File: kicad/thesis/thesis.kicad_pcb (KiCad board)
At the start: 2 copper layers, 50 x 49 mm, 13 parts, among them Q1 IRLZB8721, SW1 SW_DIP_x01, U1 INA219AxD

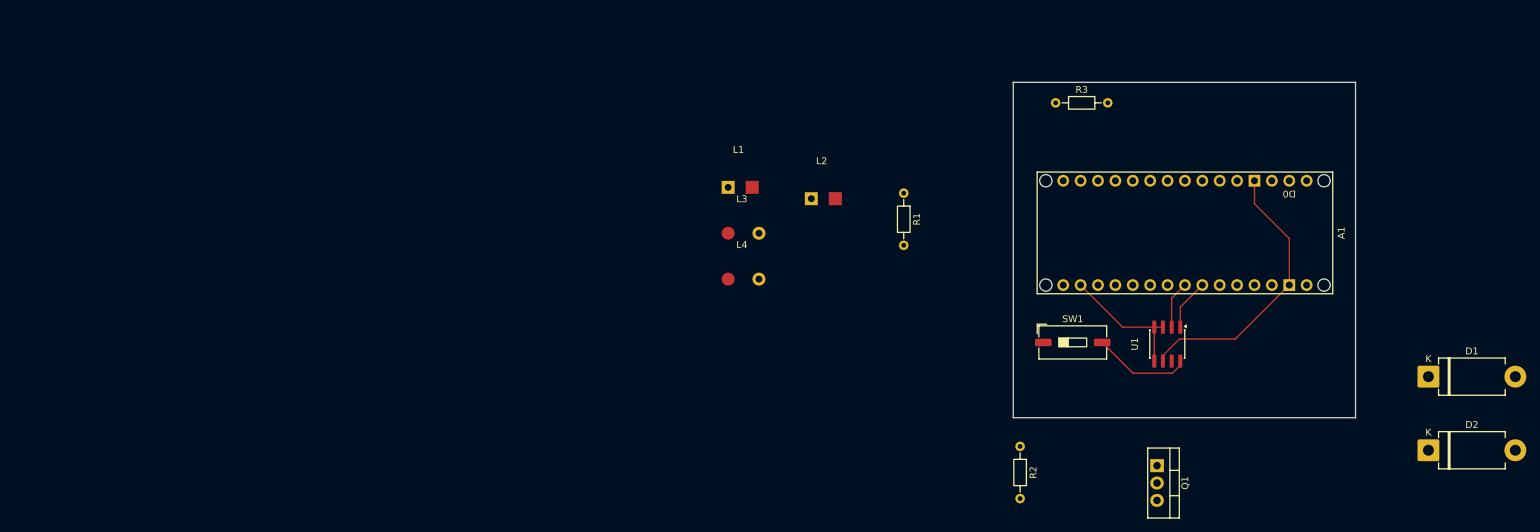
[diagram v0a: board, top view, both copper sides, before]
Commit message: Changed the PCB design
85mm x 60mm dimensions for the initial PCB layout
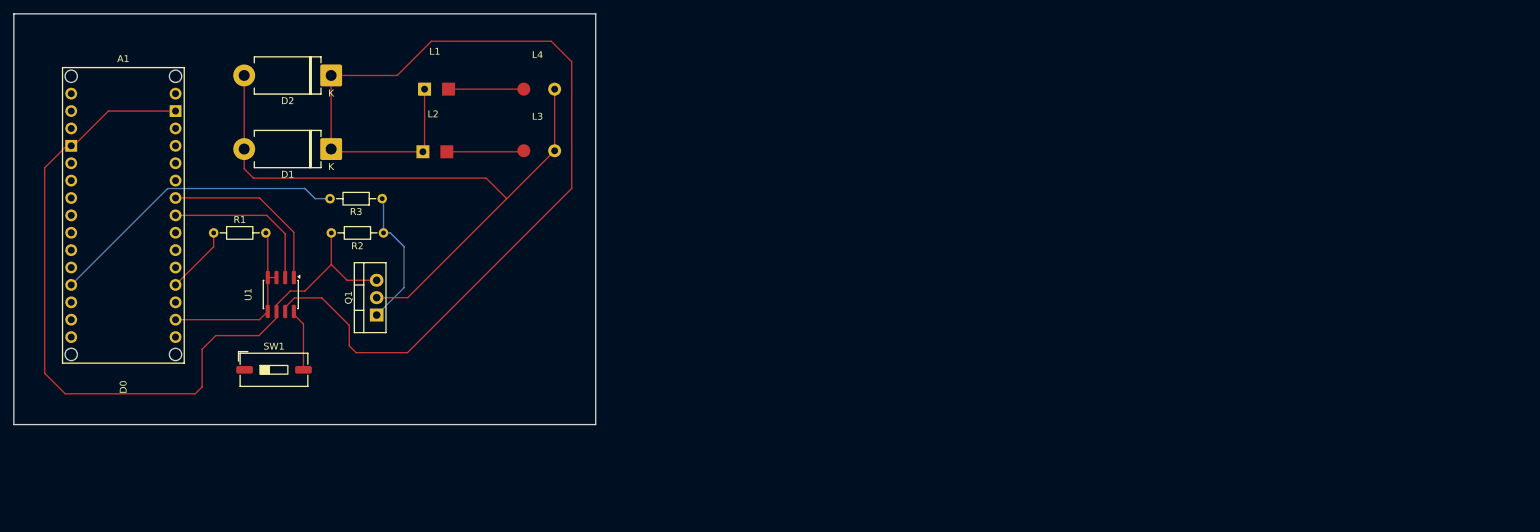
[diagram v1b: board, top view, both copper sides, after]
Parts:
- moved D2 169.4 mm to (100.3, 79.0), turned to 180 degrees
- moved D1 163.7 mm to (100.3, 89.8), turned to 180 degrees
- moved A1 134.8 mm to (70.0, 121.0), turned to 0 degrees
- moved U1 129.7 mm to (93.0, 111.0)
- moved SW1 116.8 mm to (92.0, 122.0)
- moved Q1 116.1 mm to (107.0, 114.0), turned to 90 degrees
- moved R1 101.0 mm to (83.2, 102.0), turned to 0 degrees
- moved R3 99.4 mm to (107.8, 97.0), turned to 180 degrees
- moved R2 98.1 mm to (108.0, 102.0), turned to 180 degrees
- moved L2 57.2 mm to (115.2, 85.2)
- moved L1 46.6 mm to (115.5, 76.0)
- moved L4 40.8 mm to (130.5, 76.5)
- moved L3 32.2 mm to (130.5, 85.5)
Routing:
- net Net-(D1-K): track 0.00 -> 148.6 mm
- net Net-(D1-A): track 0.00 -> 97.7 mm
- net GND: track 40.9 -> 120.1 mm
- net Net-(A1-PadD9): track 0.00 -> 44.3 mm
- net Net-(Q1-G): track 0.00 -> 20.6 mm
- net /A1: track 7.49 -> 26.0 mm
- net /A0: track 6.96 -> 23.5 mm
- net Net-(L2-Pad2): track 0.00 -> 11.3 mm
- net Net-(L1-Pad2): track 0.00 -> 11.0 mm
- net Net-(A1-PadA0): track 0.00 -> 9.91 mm
- net +3.3V: track 19.5 -> 26.8 mm
- net Net-(U1-IN+): track 14.4 -> 9.10 mm
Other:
- board size 50 x 49 mm -> 85 x 60 mm
- board text added: "Group G Thesis"

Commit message: Added Roy changes
wla pa nahuman kaon sko
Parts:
- added TH1: Thermistor_NTC, TerminalBlock_Phoenix:TerminalBlock_Phoenix_MKDS-1,5-2-5.08_1x02_P5.08mm_Horizontal, F.Cu at (104.6, 123.7)
- L1, L2: footprint Personalized-footprint:Iron-Input -> TerminalBlock_Phoenix:TerminalBlock_Phoenix_MKDS-1,5-2-5.08_1x02_P5.08mm_Horizontal
- L3, L4: footprint Personalized-footprint:Iron-Output -> TerminalBlock_Phoenix:TerminalBlock_Phoenix_MKDS-1,5-2-5.08_1x02_P5.08mm_Horizontal
- U1: footprint Package_SO:SOIC-8_3.9x4.9mm_P1.27mm -> Connector_PinSocket_1.27mm:PinSocket_1x06_P1.27mm_Vertical
- moved L2 36.5 mm to (128.2, 119.3), turned to 90 degrees
- moved L3 22.7 mm to (128.2, 108.0), turned to 90 degrees
- moved L1 22.5 mm to (128.2, 94.6), turned to 90 degrees
- moved L4 6.95 mm to (128.2, 83.0), turned to 90 degrees
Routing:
- net Net-(D1-K): track 148.6 -> 113.9 mm
- net Net-(A1-PadA0): track 9.91 -> 44.2 mm, vias 0 -> 1
- net GND: track 120.1 -> 150.1 mm
- net Net-(D1-A): track 97.7 -> 127.5 mm
- net Net-(L2-Pad2): track 11.3 -> 6.20 mm
- net Net-(L1-Pad2): track 11.0 -> 7.92 mm
